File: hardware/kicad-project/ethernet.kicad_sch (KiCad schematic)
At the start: 42 parts, among them IC7 IC_ETH_PHY_LAN8742A, J9 J_RJ45_SKT_MAG_LED, Y2 25MHZ

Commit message: Added LNB Fault pull-up and LED
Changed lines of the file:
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@@
 	)
 	(junction
+		(at 129.54 139.7)
+		(diameter 0)
+		(color 0 0 0 0)
+	)
+	(junction
 		(at 158.75 57.15)
 		(diameter 0)
@@
 	(wire
 		(pts
+			(xy 129.54 139.7) (xy 127 139.7)
+		)
+		(stroke
+			(width 0)
+			(type default)
+		)
+	)
+	(wire
+		(pts
 			(xy 17.78 29.21) (xy 24.13 29.21)
 		)
@@
 	(wire
 		(pts
-			(xy 139.7 139.7) (xy 127 139.7)
+			(xy 139.7 139.7) (xy 129.54 139.7)
 		)
 		(stroke
@@
 	(symbol
 		(lib_id "power:GND")
-		(at 127 139.7 0)
+		(at 129.54 139.7 0)
 		(unit 1)
 		(body_style 1)
@@
 		(fields_autoplaced yes)
 		(property "Reference" "#PWR066"
-			(at 127 146.05 0)
+			(at 129.54 146.05 0)
 			(hide yes)
 			(show_name no)
@@
 		)
 		(property "Value" "GND"
-			(at 127 144.78 0)
+			(at 129.54 144.78 0)
 			(show_name no)
 			(do_not_autoplace no)
@@
 		)
 		(property "Footprint" ""
-			(at 127 139.7 0)
+			(at 129.54 139.7 0)
 			(hide yes)
 			(show_name no)
@@
 		)
 		(property "Datasheet" ""
-			(at 127 139.7 0)
+			(at 129.54 139.7 0)
 			(hide yes)
 			(show_name no)
@@
 		)
 		(property "Description" "Power symbol creates a global label with name \"GND\" , ground"
-			(at 127 139.7 0)
+			(at 129.54 139.7 0)
 			(hide yes)
 			(show_name no)

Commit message: Add fiducials
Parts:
- renumbered C37 to C41, C38 to C42, C39 to C43, C40 to C44, C41 to C45, C42 to C46, C43 to C47, C44 to C48, R18 to R21, R19 to R22, R20 to R23, R21 to R24, R22 to R25, R23 to R26, R24 to R27, R25 to R28, R26 to R29, R27 to R30, R28 to R31, R29 to R32, R30 to R33, R31 to R34, R32 to R35, R33 to R36, R34 to R37, R35 to R38, R36 to R39, R37 to R40

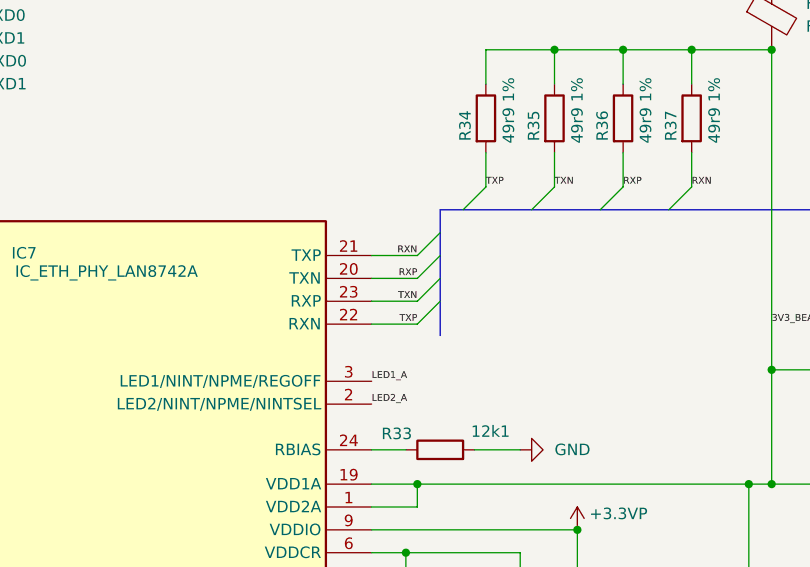
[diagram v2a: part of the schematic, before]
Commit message: Corrected thermal/EMC issues
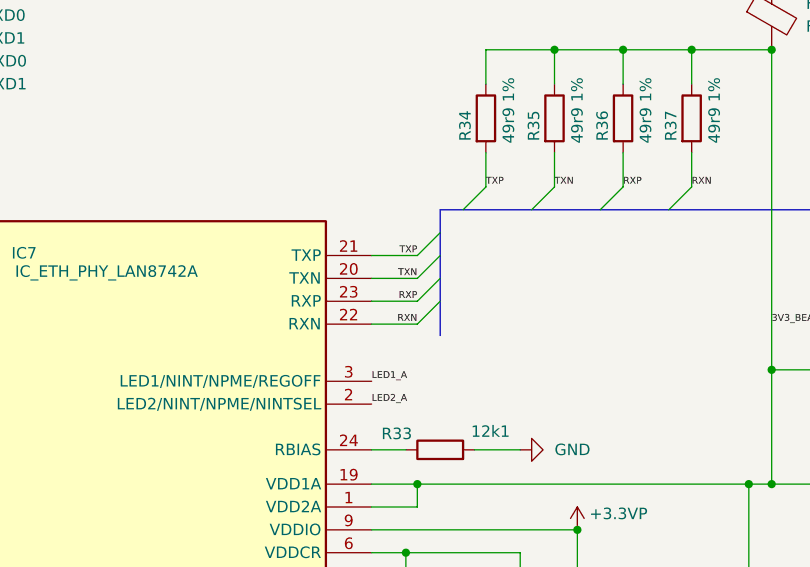
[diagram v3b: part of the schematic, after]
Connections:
- net RXN: now also IC7.22 (RXN); no longer IC7.21 (TXP)
- net RXP: now also IC7.23 (RXP); no longer IC7.20 (TXN)
- net TXN: now also IC7.20 (TXN); no longer IC7.23 (RXP)
- net TXP: now also IC7.21 (TXP); no longer IC7.22 (RXN)
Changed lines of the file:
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@@
-		)
-	)
-	(label "RXN"
-		(at 128.27 80.01 180)
-		(effects
-			(font
-				(size 0.762 0.762)
-			)
-			(justify right bottom)
 		)
 	)
@@
 		)
 	)
+	(label "RXN"
+		(at 128.27 87.63 180)
+		(effects
+			(font
+				(size 0.762 0.762)
+			)
+			(justify right bottom)
+		)
+	)
 	(label "LED2_A"
 		(at 260.35 82.55 0)
@@
 		)
 	)
+	(label "TXN"
+		(at 128.27 82.55 180)
+		(effects
+			(font
+				(size 0.762 0.762)
+			)
+			(justify right bottom)
+		)
+	)
+	(label "TXP"
+		(at 128.27 80.01 180)
+		(effects
+			(font
+				(size 0.762 0.762)
+			)
+			(justify right bottom)
+		)
+	)
 	(label "REF_CLK"
 		(at 17.78 29.21 0)
@@
 		)
 	)
+	(label "RXP"
+		(at 128.27 85.09 180)
+		(effects
+			(font
+				(size 0.762 0.762)
+			)
+			(justify right bottom)
+		)
+	)
 	(label "RXD0"
 		(at 17.78 90.17 0)
@@
 		)
 	)
-	(label "RXP"
-		(at 128.27 82.55 180)
-		(effects
-			(font
-				(size 0.762 0.762)
-			)
-			(justify right bottom)
-		)
-	)
 	(label "LED1_A"
 		(at 243.84 90.17 0)
@@
 		)
 	)
-	(label "TXP"
-		(at 128.27 87.63 180)
-		(effects
-			(font
-				(size 0.762 0.762)
-			)
-			(justify right bottom)
-		)
-	)
 	(label "RXP"
 		(at 151.13 72.39 0)
@@
 		)
 	)
-	(label "TXN"
-		(at 128.27 85.09 180)
-		(effects
-			(font
-				(size 0.762 0.762)
-			)
-			(justify right bottom)
-		)
-	)

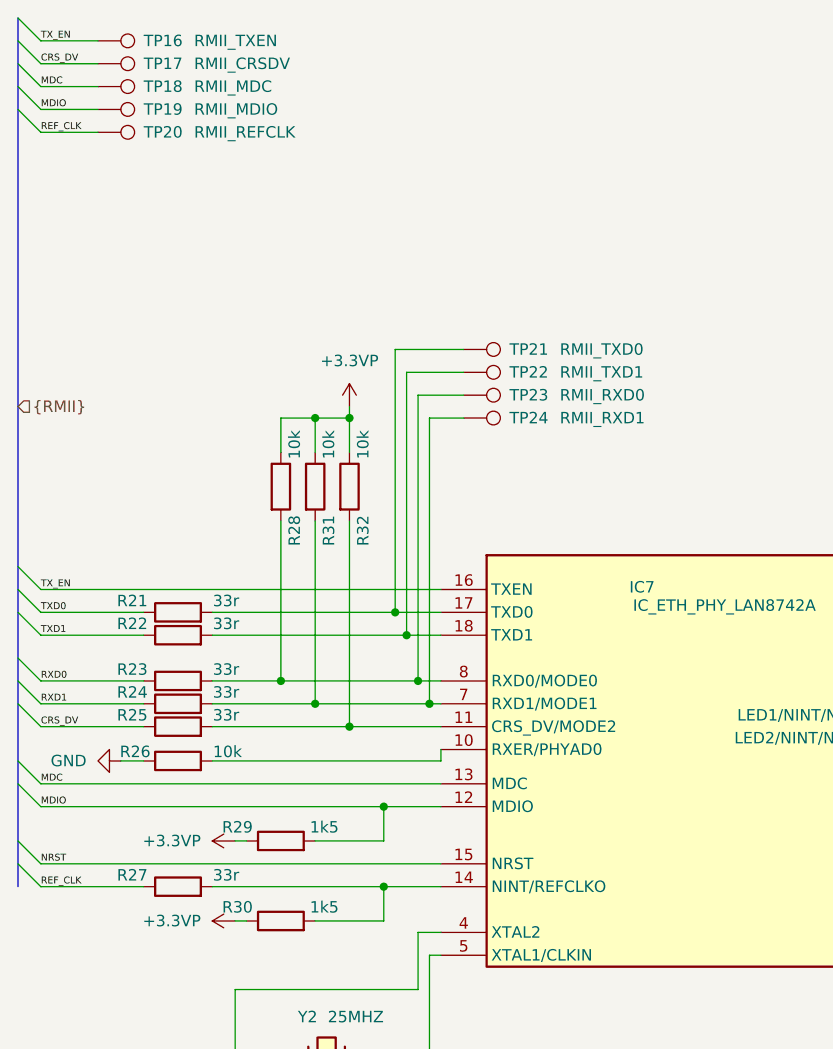
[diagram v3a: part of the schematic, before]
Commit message: Removed unnecessary test points
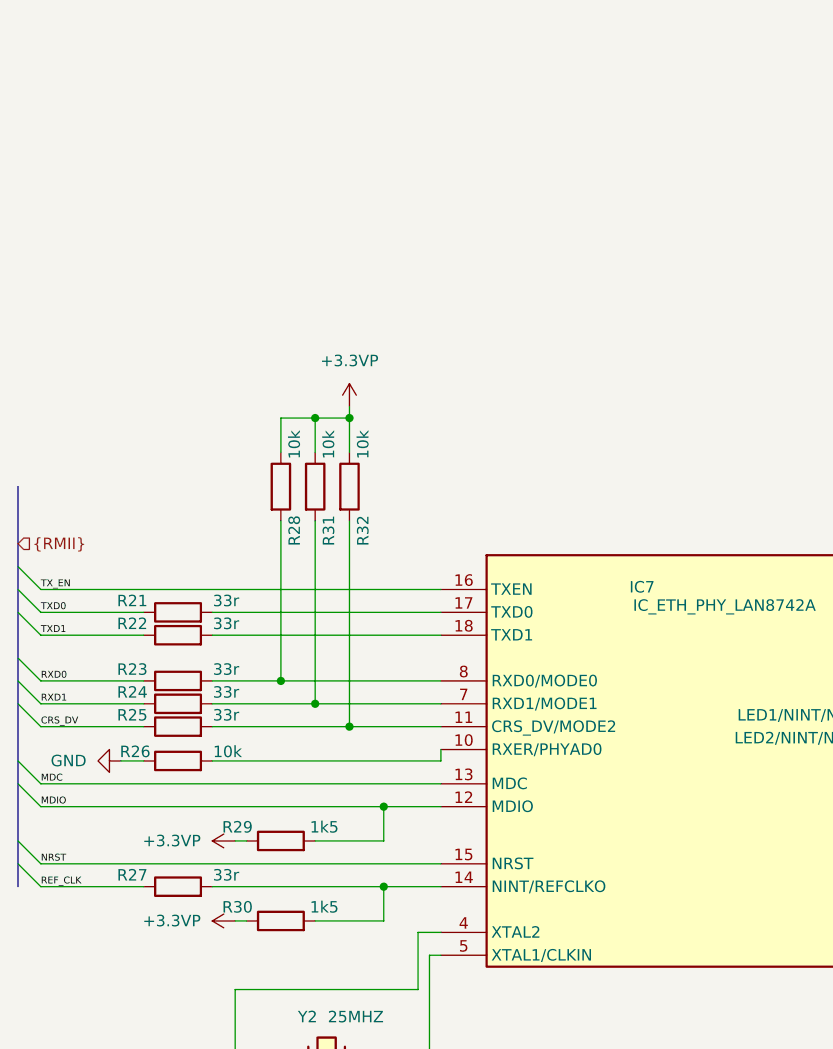
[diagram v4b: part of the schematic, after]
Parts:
- removed TP16: RMII_TXEN, ebnx_footprints:TestPoint_THTPad_D1.0mm_Drill0.5mm_annotated, symbol ebnx_symbols:TestPoint_Annotated_Silkscreen
- removed TP17: RMII_CRSDV, ebnx_footprints:TestPoint_THTPad_D1.0mm_Drill0.5mm_annotated, symbol ebnx_symbols:TestPoint_Annotated_Silkscreen
- removed TP18: RMII_MDC, ebnx_footprints:TestPoint_THTPad_D1.0mm_Drill0.5mm_annotated, symbol ebnx_symbols:TestPoint_Annotated_Silkscreen
- removed TP19: RMII_MDIO, ebnx_footprints:TestPoint_THTPad_D1.0mm_Drill0.5mm_annotated, symbol ebnx_symbols:TestPoint_Annotated_Silkscreen
- removed TP20: RMII_REFCLK, ebnx_footprints:TestPoint_THTPad_D1.0mm_Drill0.5mm_annotated, symbol ebnx_symbols:TestPoint_Annotated_Silkscreen
- removed TP21: RMII_TXD0, ebnx_footprints:TestPoint_THTPad_D1.0mm_Drill0.5mm_annotated, symbol ebnx_symbols:TestPoint_Annotated_Silkscreen
- removed TP22: RMII_TXD1, ebnx_footprints:TestPoint_THTPad_D1.0mm_Drill0.5mm_annotated, symbol ebnx_symbols:TestPoint_Annotated_Silkscreen
- removed TP23: RMII_RXD0, ebnx_footprints:TestPoint_THTPad_D1.0mm_Drill0.5mm_annotated, symbol ebnx_symbols:TestPoint_Annotated_Silkscreen
- removed TP24: RMII_RXD1, ebnx_footprints:TestPoint_THTPad_D1.0mm_Drill0.5mm_annotated, symbol ebnx_symbols:TestPoint_Annotated_Silkscreen
